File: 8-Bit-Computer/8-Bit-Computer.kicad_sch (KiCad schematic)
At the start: 86 parts, among them J1 XLR3_Switched, J2 XLR3_Switched, SW1 SW_Push, SW2 SW_DIP_x04, SW3 SW_DIP_x08, SW4 SW_Push, U1 NA555D, U10 74LS283, U11 74HC245, U12 74HC86, U13 74HC86, U14 74HC245, U15 HM62256BLP, U16 74HC245, U17 74157, U18 74157, U19 74157, U2 AMS1117-5.0, U20 74HC00, U21 74157, U22 74173, U23 74LS377, U24 74LS377, U25 74LS377, U26 74HC245, U27 74LS161, U28 74HC245, U29 HDSP-7503, U3 74HC00, U4 LM555xM, U5 NA555D, U6 74HC00, U7 74HC245, U8 74HC245, U9 74LS283

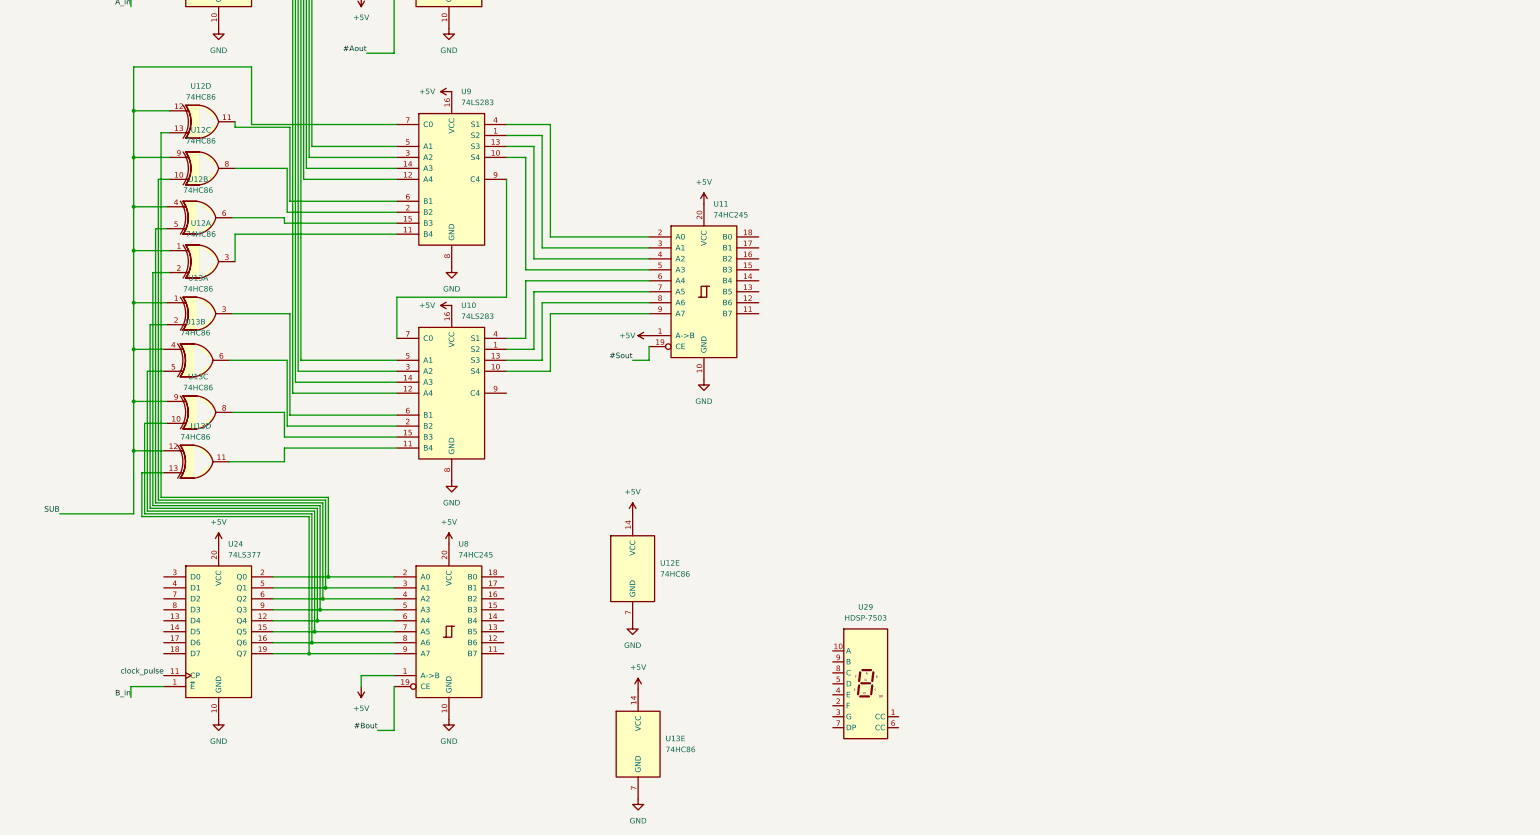
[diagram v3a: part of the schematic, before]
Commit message: added eeprom and 7-seg display
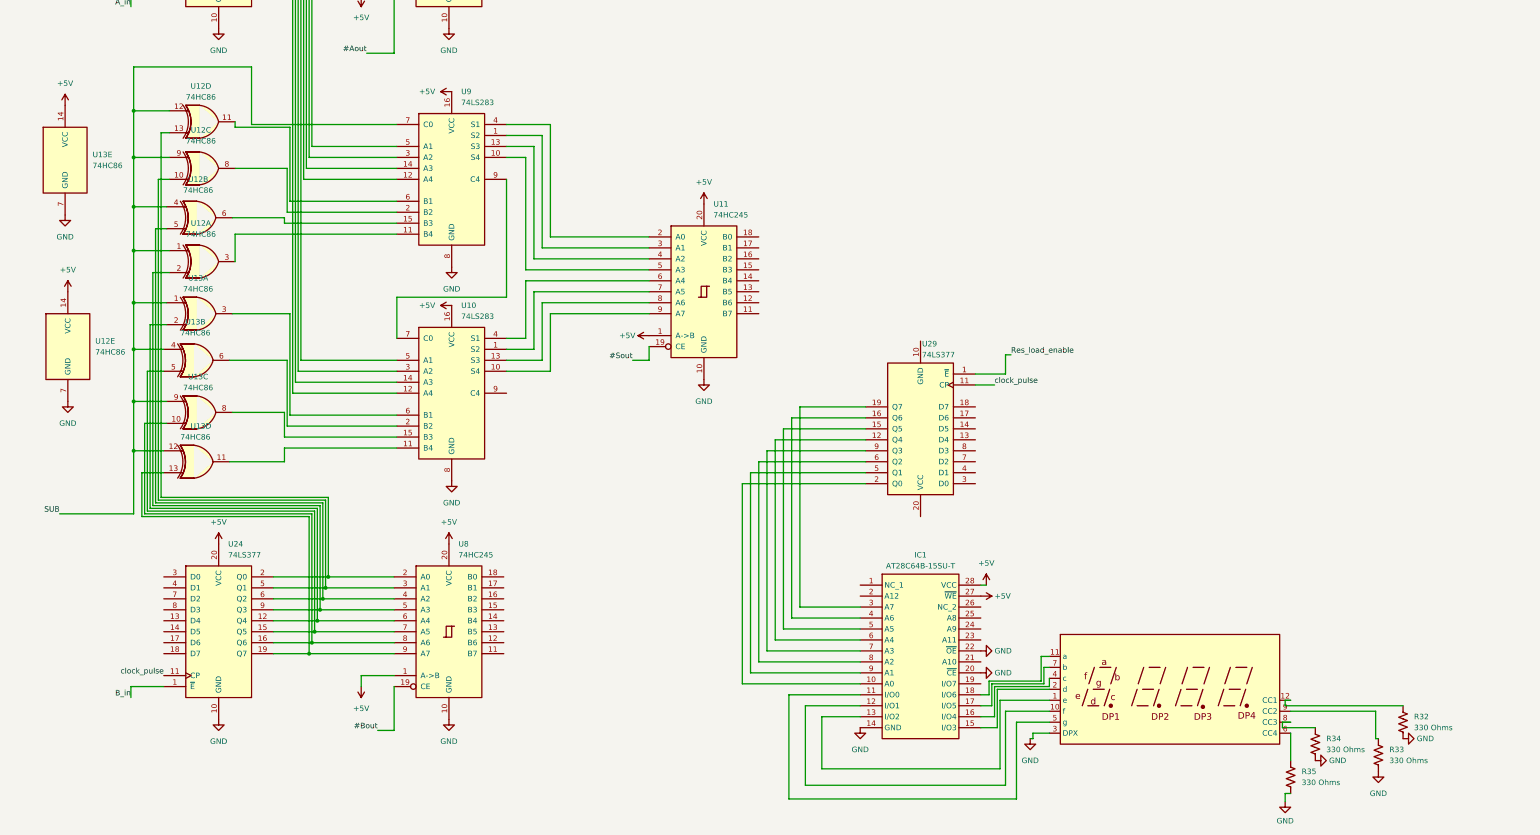
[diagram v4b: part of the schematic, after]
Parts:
- removed U29: HDSP-7503, Display_7Segment:HDSP-A151, symbol Display_Character:HDSP-7503
- added IC1: AT28C64B-15SU-T, SOIC127P1032X265-28N, symbol New_Library:AT28C64B-15SU-T
- added R32, R33, R34, R35: 330 Ohms, symbol Device:R_US
- added U29: 74LS377, symbol 74xx:74LS377
- added U30: CC56-12GWA, Display_7Segment:CC56-12GWA, symbol Display_Character:CC56-12GWA
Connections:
- net +5V: now also IC1.27 (~{WE}), IC1.28 (VCC)
- net GND: now also IC1.14 (GND), IC1.20 (~{CE}), IC1.22 (~{OE}), R32.1, R33.1, R34.1, R35.1, U30.3 (DPX)
- net clock_pulse: now also U29.11 (CP)
- new net: IC1.6 (A4), U29.12 (Q4)
- new net: IC1.5 (A5), U29.15 (Q5)
- new net: IC1.4 (A6), U29.16 (Q6)
- new net: IC1.3 (A7), U29.19 (Q7)
- new net: IC1.10 (A0), U29.2 (Q0)
- new net: IC1.9 (A1), U29.5 (Q1)
- new net: IC1.8 (A2), U29.6 (Q2)
- new net: IC1.7 (A3), U29.9 (Q3)
- new net: R35.2, U30.6 (CC4)
- new net: R33.2, U30.9 (CC2)
- new net: IC1.11 (I/O0), U30.5 (g)
- new net: IC1.12 (I/O1), U30.10 (f)
- new net: IC1.13 (I/O2), U30.1 (e)
- new net: IC1.15 (I/O3), U30.2 (d)
- new net: IC1.16 (I/O4), U30.4 (c)
- new net: IC1.17 (I/O5), U30.7 (b)
- new net: IC1.18 (I/O6), U30.11 (a)
- new net: R32.2, U30.12 (CC1)
- new net: R34.2, U30.8 (CC3)
- new net Res_load_enable: U29.1 (~{E})
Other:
- moved on the sheet: U12E, U13E

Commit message: Cleaned up Current Schematics
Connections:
- net +5V: now also R3.1, R4.2, R6.1; no longer R3.2, R4.1, R6.2
- net GND: now also C3.1; no longer C3.2
- net BUS3: now reaches U28.15 (B3)
- net BUS3: now also U23.8 (D3), U24.8 (D3), U27.6 (D3), U7.15 (B3), U8.15 (B3)
- net BUS2: now reaches U28.16 (B2)
- net BUS2: now also U23.7 (D2), U24.7 (D2), U27.5 (D2), U7.16 (B2), U8.16 (B2)
- net BUS1: now reaches U28.17 (B1)
- net BUS1: now also U23.4 (D1), U24.4 (D1), U27.4 (D1), U7.17 (B1), U8.17 (B1)
- net BUS0: now reaches U28.18 (B0)
- net BUS0: now also U23.3 (D0), U24.3 (D0), U27.3 (D0), U7.18 (B0), U8.18 (B0)
- net at J1.NO, U5.4 (R): now also R6.2; no longer R6.1
- net BUS4: now reaches U23.13 (D4)
- net BUS4: now also U24.13 (D4), U7.14 (B4), U8.14 (B4)
- net BUS5: now reaches U23.14 (D5)
- net BUS5: now also U24.14 (D5), U7.13 (B5), U8.13 (B5)
- net BUS6: now reaches U23.17 (D6)
- net BUS6: now also U24.17 (D6), U7.12 (B6), U8.12 (B6)
- net BUS7: now reaches U23.18 (D7)
- net BUS7: now also U24.18 (D7), U7.11 (B7), U8.11 (B7)
- net at U1.5 (CV): now also C3.2; no longer C3.1
- net at SW1.2, U4.2 (TR): now also R3.2; no longer R3.1
- net at C5.1, U4.6 (THR), U4.7 (DIS): now also R4.1; no longer R4.2
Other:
- note removed: "ALU and Registers"
- moved on the sheet: C1, C2, C3, C4, C5, C6, C7, D10, D11, D2, D8, D9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

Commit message: Cleaned up RAM module
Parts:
- removed R21, R22, R23, R24: 1 Mohm, symbol Device:R_US
- removed U22: 74173, symbol 74xx_IEEE:74173
- added R36, R37, R38, R39: 1 Mohm, symbol Device:R_US
- added U31: 74LS377, symbol 74xx:74LS377
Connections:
- net +5V: now also U14.1 (A->B), U16.10 (GND), U18.16 (VCC), R36.2, R37.2, R38.2, R39.2, U31.20 (VCC); no longer U16.20 (VCC)
- net Addr_in: now also U31.1 (~{E})
- net BUS0: now also U16.18 (B0), U17.3 (I1a), U25.3 (D0), U26.18 (B0), U31.3 (D0)
- net BUS1: now also U16.17 (B1), U17.6 (I1b), U25.4 (D1), U26.17 (B1), U31.4 (D1)
- net BUS2: now also U16.16 (B2), U17.13 (I1c), U25.7 (D2), U26.16 (B2), U31.7 (D2)
- net BUS3: now also U16.15 (B3), U17.10 (I1d), U25.8 (D3), U26.15 (B3), U31.8 (D3)
- net BUS4: now also U16.14 (B4), U18.3 (I1a), U25.13 (D4), U26.14 (B4)
- net BUS5: now also U16.13 (B5), U18.6 (I1b), U25.14 (D5), U26.13 (B5)
- net BUS6: now also U16.12 (B6), U18.13 (I1c), U25.17 (D6), U26.12 (B6)
- net BUS7: now also U16.11 (B7), U18.10 (I1d), U25.18 (D7), U26.11 (B7)
- net GND: now also SW2.1, SW2.2, SW2.3, SW2.4, U16.20 (VCC), U18.15 (~{EN}), U18.8 (GND), U19.10 (I1d), U19.11 (I0d), U19.13 (I1c), U19.14 (I0c), U19.5 (I0b), U19.6 (I1b), U26.2 (A0), U26.3 (A1), U26.4 (A2), U26.5 (A3), U31.10 (GND), U31.13 (D4), U31.14 (D5), U31.17 (D6), U31.18 (D7); no longer SW2.5, SW2.6, SW2.7, SW2.8, U14.1 (A->B), U16.10 (GND)
- net clock_pulse: now also C8.1, U31.11 (CP); no longer C8.2
- net PROG: now reaches D7.1 (K), J2.NO, U17.1 (A/B), U19.1 (A/B)
- net PROG: now also U18.1 (A/B), U21.1 (A/B)
- net MS5: now reaches SW3.11, U18.5 (I0b)
- net MS5: now also R36.1
- net at U21.2 (I0a): now also R8.1, SW2.5
- net at U21.5 (I0b): now also R9.1, SW2.6
- net at U21.14 (I0c): now also R10.1, SW2.7
- net at U25.12 (Q4): no longer U26.6 (A4)
- net at U25.15 (Q5): no longer U26.7 (A5)
- net at U25.16 (Q6): no longer U26.8 (A6)
- net at U25.19 (Q7): no longer U26.9 (A7)
- net at U25.2 (Q0): now also U26.6 (A4); no longer U26.2 (A0)
- net at U25.5 (Q1): now also U26.7 (A5); no longer U26.3 (A1)
- net at U25.6 (Q2): now also U26.8 (A6); no longer U26.4 (A2)
- net at U25.9 (Q3): now also U26.9 (A7); no longer U26.5 (A3)
- net MS7: now reaches SW3.9, U18.11 (I0d)
- net MS7: now also R38.1
- net at U18.12 (Qc): now also U14.8 (A6); no longer U14.12 (B6)
- net MS6: now reaches SW3.10, U18.14 (I0c)
- net MS6: now also R37.1
- net MS4: now reaches SW3.12, U18.2 (I0a)
- net MS4: now also R19.1
- net at U18.4 (Qa): now also U14.6 (A4); no longer U14.14 (B4)
- net at U18.7 (Qb): now also U14.7 (A5); no longer U14.13 (B5)
- net at U18.9 (Qd): now also U14.9 (A7); no longer U14.11 (B7)
- net at R26.1, U20.1: now also C8.2; no longer C8.1
- net MS3: now reaches SW3.13, U17.11 (I0d)
- net MS3: now also R39.1; no longer R20.1
- net MS2: now reaches SW3.14, U17.14 (I0c)
- net MS2: now also R20.1; no longer R19.1
- net MS1: now reaches R18.1, SW3.15, U17.5 (I0b)
- net MS0: now reaches R17.1, SW3.16, U17.2 (I0a)
- net at U17.12 (Qc): now also U14.4 (A2); no longer U14.16 (B2)
- net at U17.4 (Qa): now also U14.2 (A0); no longer U14.18 (B0)
- net at U17.7 (Qb): now also U14.3 (A1); no longer U14.17 (B1)
- net at U17.9 (Qd): now also U14.5 (A3); no longer U14.15 (B3)
- net at D1.1 (K), J2.NC: no longer U21.1 (A/B)
- net at D4.2 (A), U21.12 (Qc): now also U15.9 (A1); no longer U15.8 (A2)
- net at D3.2 (A), U21.9 (Qd): now also U15.10 (A0); no longer U15.7 (A3)
- net at R25.1, SW4.2: now also U19.2 (I0a)
- net WRAM: now reaches U14.19 (CE), U15.27 (~{WE}), U19.4 (Qa)
- net at U15.11 (Q0), U16.2 (A0): now also U14.18 (B0); no longer U14.2 (A0)
- net at U15.12 (Q1), U16.3 (A1): now also U14.17 (B1); no longer U14.3 (A1)
- net at U15.13 (Q2), U16.4 (A2): now also U14.16 (B2); no longer U14.4 (A2)
- net at U15.15 (Q3), U16.5 (A3): now also U14.15 (B3); no longer U14.5 (A3)
- net at U15.16 (Q4), U16.6 (A4): now also U14.14 (B4); no longer U14.6 (A4)
- net at U15.17 (Q5), U16.7 (A5): now also U14.13 (B5); no longer U14.7 (A5)
- net at U15.18 (Q6), U16.8 (A6): now also U14.12 (B6); no longer U14.8 (A6)
- net at U15.19 (Q7), U16.9 (A7): now also U14.11 (B7); no longer U14.9 (A7)
- new net: U21.10 (I1d), U31.9 (Q3)
- new net: R11.1, SW2.8, U21.11 (I0d)
- new net: U21.13 (I1c), U31.6 (Q2)
- new net: U21.3 (I1a), U31.2 (Q0)
- new net: D5.2 (A), U15.7 (A3), U21.4 (Qa)
- new net: U21.6 (I1b), U31.5 (Q1)
- new net: D6.2 (A), U15.8 (A2), U21.7 (Qb)
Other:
- note removed: "RAM"
- moved on the sheet: C8, D1, D7, IC1, J2B, R10, R11, R12, R25, R26, R32, R33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

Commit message: completed ALU and most of the control logic
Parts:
- removed R32, R33, R34, R35: 330 Ohms, symbol Device:R_US
- removed U30: CC56-12GWA, Display_7Segment:CC56-12GWA, symbol Display_Character:CC56-12GWA
- removed U8: 74HC245, symbol 74xx:74HC245
- added C10: 0.1 uF, symbol Device:C
- added C9: 0.01 uF, symbol Device:C
- added IC2, IC3: AT28C64B-15SU-T, SOIC127P1032X265-28N, symbol New_Library:AT28C64B-15SU-T
- added J3: XLR3_Switched, symbol Connector_Audio:XLR3_Switched
- added R21: 100 kOhm, symbol Device:R
- added R22: 1 kOhm, symbol Device:R
- added R23: 10 Kohm, symbol Device:R_US
- added SW5: SW_Push, symbol Switch:SW_Push
- added U22, U30, U32, U33: HDSP-7403, Display_7Segment:HDSP-7401, symbol Display_Character:HDSP-7403
- added U34: 74LS107, symbol 74xx:74LS107
- added U35: NA555D, Package_SO:SOIC-8_3.9x4.9mm_P1.27mm, symbol Timer:NA555D
- added U36: 74LS139, symbol 74xx:74LS139
- added U37: 74LS161, symbol 74xx:74LS161
- added U38: 74LS138, symbol 74xx:74LS138
- added U39: 74LS08, symbol 74xx:74LS08
- added U40, U41: 74LS04, symbol 74xx:74LS04
- added U42: 74LS377, symbol 74xx:74LS377
- added U8: 74LS02, symbol 74xx:74LS02
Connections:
- net #J: now also U41.4
- net +5V: now also U27.1 (~{MR}), U29.20 (VCC), IC2.27 (~{WE}), IC2.28 (VCC), IC3.27 (~{WE}), IC3.28 (VCC), J3.NC, R22.2, SW5.1, U34.1 (J), U34.10 (~{R}), U34.11 (K), U34.13 (~{R}), U34.14 (VCC), U34.4 (K), U34.8 (J), U35.4 (R), U35.8 (VCC), U36.1 (E), U36.16 (VCC), U37.10 (CET), U37.16 (VCC), U37.7 (CEP), U37.9 (~{PE}), U38.16 (VCC), U38.6 (E3), U39.14 (VCC), U40.14 (VCC), U41.14 (VCC), U42.20 (VCC), U8.14 (VCC)
- net BUS0: now also U11.18 (B0), U29.3 (D0)
- net BUS1: now also U11.17 (B1), U29.4 (D1)
- net BUS2: now also U11.16 (B2), U29.7 (D2)
- net BUS3: now also U11.15 (B3), U29.8 (D3)
- net BUS4: now also U11.14 (B4), U29.13 (D4)
- net BUS5: now also U11.13 (B5), U29.14 (D5)
- net BUS6: now also U11.12 (B6), U29.17 (D6)
- net BUS7: now also U11.11 (B7), U29.18 (D7)
- net GND: now also IC1.2 (A12), IC1.23 (A11), U29.10 (GND), C10.1, C9.2, IC2.14 (GND), IC2.2 (A12), IC2.20 (~{CE}), IC2.21 (A10), IC2.22 (~{OE}), IC2.23 (A11), IC2.24 (A9), IC3.14 (GND), IC3.2 (A12), IC3.20 (~{CE}), IC3.21 (A10), IC3.22 (~{OE}), IC3.23 (A11), IC3.24 (A9), J3.NO, R23.1, U22.7 (DP), U30.7 (DP), U32.7 (DP), U33.7 (DP), U34.7 (GND), U35.1 (GND), U36.13 (A1), U36.14 (A0), U36.15 (E), U36.8 (GND), U37.8 (GND), U38.4 (E1), U38.5 (E2), U38.8 (GND), U39.7 (GND), U40.7 (GND), U41.7 (GND), U42.10 (GND), U42.13 (D4), U42.14 (D5), U42.17 (D6), U42.18 (D7), U42.7 (D2), U42.8 (D3), U8.7 (GND)
- net HLT: now also IC2.19 (I/O7)
- net clock_pulse: now also U37.2 (CP), U42.11 (CP)
- net IR_4: now reaches U25.12 (Q4)
- net IR_4: now also IC2.7 (A3), IC3.7 (A3)
- net IR_5: now reaches U25.15 (Q5)
- net IR_5: now also IC2.6 (A4), IC3.6 (A4)
- net IR_6: now reaches U25.16 (Q6)
- net IR_6: now also IC2.5 (A5), IC3.5 (A5)
- net IR_7: now reaches U25.19 (Q7)
- net IR_7: now also IC2.4 (A6), IC3.4 (A6)
- net ALU_0: now reaches U11.2 (A0), U9.4 (S1)
- net ALU_0: now also U8.2
- net ALU_1: now reaches U11.3 (A1), U9.1 (S2)
- net ALU_1: now also U8.3
- net ALU_2: now reaches U11.4 (A2), U9.13 (S3)
- net ALU_2: now also U8.5
- net ALU_3: now reaches U11.5 (A3), U9.10 (S4)
- net ALU_3: now also U8.6
- net ALU_4: now reaches U10.4 (S1), U11.6 (A4)
- net ALU_4: now also U8.8
- net ALU_5: now reaches U10.1 (S2), U11.7 (A5)
- net ALU_5: now also U8.9
- net ALU_6: now reaches U10.13 (S3), U11.8 (A6)
- net ALU_6: now also U8.11
- net ALU_7: now reaches U10.10 (S4), U11.9 (A7)
- net ALU_7: now also U8.12
- net #CLR: now reaches U20.11
- net #CLR: now also U20.4, U20.5, U20.9
- net at U20.12: now also U20.13, R23.2, SW5.2
- net LCD_G: now reaches IC1.11 (I/O0)
- net LCD_G: now also U22.3 (G), U30.3 (G), U32.3 (G), U33.3 (G)
- net LCD_F: now reaches IC1.12 (I/O1)
- net LCD_F: now also U22.2 (F), U30.2 (F), U32.2 (F), U33.2 (F)
- net LCD_E: now reaches IC1.13 (I/O2)
- net LCD_E: now also U22.4 (E), U30.4 (E), U32.4 (E), U33.4 (E)
- net LCD_B: now reaches IC1.15 (I/O3)
- net LCD_B: now also IC1.17 (I/O5), U22.5 (D), U22.9 (B), U30.5 (D), U30.9 (B), U32.5 (D), U32.9 (B), U33.5 (D), U33.9 (B)
- net LCD_C: now reaches IC1.16 (I/O4)
- net LCD_C: now also U22.8 (C), U30.8 (C), U32.8 (C), U33.8 (C)
- net LCD_A: now reaches IC1.18 (I/O6)
- net LCD_A: now also U22.10 (A), U30.10 (A), U32.10 (A), U33.10 (A)
- net at IC1.21 (A10): now also J3.N
- net at IC1.24 (A9): now also U34.6 (~{Q}), U36.3 (A1)
- net at IC1.25 (A8): now also U34.2 (~{Q}), U34.9 (C), U36.2 (A0)
- net CLR: now reaches U20.6
- net at U20.10: now also U38.10 (O5)
- net at U20.8: now also U41.13
- net at U10.9 (C4): now also U42.3 (D0)
- net #Aout renamed #AO
- net #AO: now also U40.2
- net #Sout renamed #EO
- net #EO: now also U41.10
- net A_in renamed #AI
- net #AI: now also U40.4
- net B_in renamed #BI
- net #BI: now also U41.8
- new net: C10.2, U35.5 (CV)
- new net: U39.5, U8.13
- new net: U34.12 (C), U35.3 (Q)
- new net: U22.1 (CC), U22.6 (CC), U36.4 (O0)
- new net: U30.1 (CC), U30.6 (CC), U36.5 (O1)
- new net: U32.1 (CC), U32.6 (CC), U36.6 (O2)
- new net: U33.1 (CC), U33.6 (CC), U36.7 (O3)
- new net: R21.2, R22.1, U35.7 (DIS)
- new net: C9.1, R21.1, U35.2 (TR), U35.6 (THR)
- new net: U37.1 (~{MR}), U41.12
- new net: U39.4, U8.10
- new net: U39.10, U39.6
- new net: U39.1, U8.1
- new net: U39.2, U8.4
- new net: U39.3, U39.9
- new net: U39.8, U42.4 (D1)
- new net #CO: U41.6
- new net #FI: U41.2, U42.1 (~{E})
- new net #II: U40.6
- new net #IO: U40.8
- new net #MI: U40.12
- new net #RO: U40.10
- new net AI: IC2.12 (I/O1), U40.3
- new net AO: IC2.11 (I/O0), U40.1
- new net BI: IC3.17 (I/O5), U41.9
- new net CE: IC3.15 (I/O3)
- new net CF: IC2.3 (A7), IC3.3 (A7), U42.2 (Q0)
- new net CL_IB1: IC2.10 (A0), IC3.10 (A0), U37.14 (Q0), U38.1 (A0)
- new net CL_IB2: IC2.9 (A1), IC3.9 (A1), U37.13 (Q1), U38.2 (A1)
- new net CL_IB3: IC2.8 (A2), IC3.8 (A2), U37.12 (Q2), U38.3 (A2)
- new net CO: IC3.13 (I/O2), U41.5
- new net EO: IC3.19 (I/O7), U41.11
- new net FI: IC3.11 (I/O0), U41.1
- new net II: IC2.13 (I/O2), U40.5
- new net IO: IC2.15 (I/O3), U40.9
- new net J: IC3.12 (I/O1), U41.3
- new net MI: IC2.18 (I/O6), U40.13
- new net OI: IC3.16 (I/O4)
- new net RI: IC2.17 (I/O5)
- new net RO: IC2.16 (I/O4), U40.11
- new net SU: IC3.18 (I/O6)
- new net ZF: IC2.25 (A8), IC3.25 (A8), U42.5 (Q1)
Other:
- moved on the sheet: C8, D1, D3, D4, D5, D6, D7, IC1, J2B, R10, R11, R12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
